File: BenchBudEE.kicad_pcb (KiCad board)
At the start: 4 copper layers, 165.1 x 63.5 mm, 134 parts, among them K1 1461069-5, P1 24-pin Mini-Fit Jr., P2 CONN_2, P3 CONN_3X2, P4 12-pin Terminal Block, P5 3-pin TB, Q1 2N3404, Q2 DMN65D8L-7, Q3 AOD476, Q4 AOD476, SW1 Power Switch, U1 LTV-816S, U10 LMT84, U11 OPA4170, U2 AP5726, U3 LM317T, U4 LM317T, U5 LM337T, U6 LM337T, U8 MCP4801, U9 MCP3901

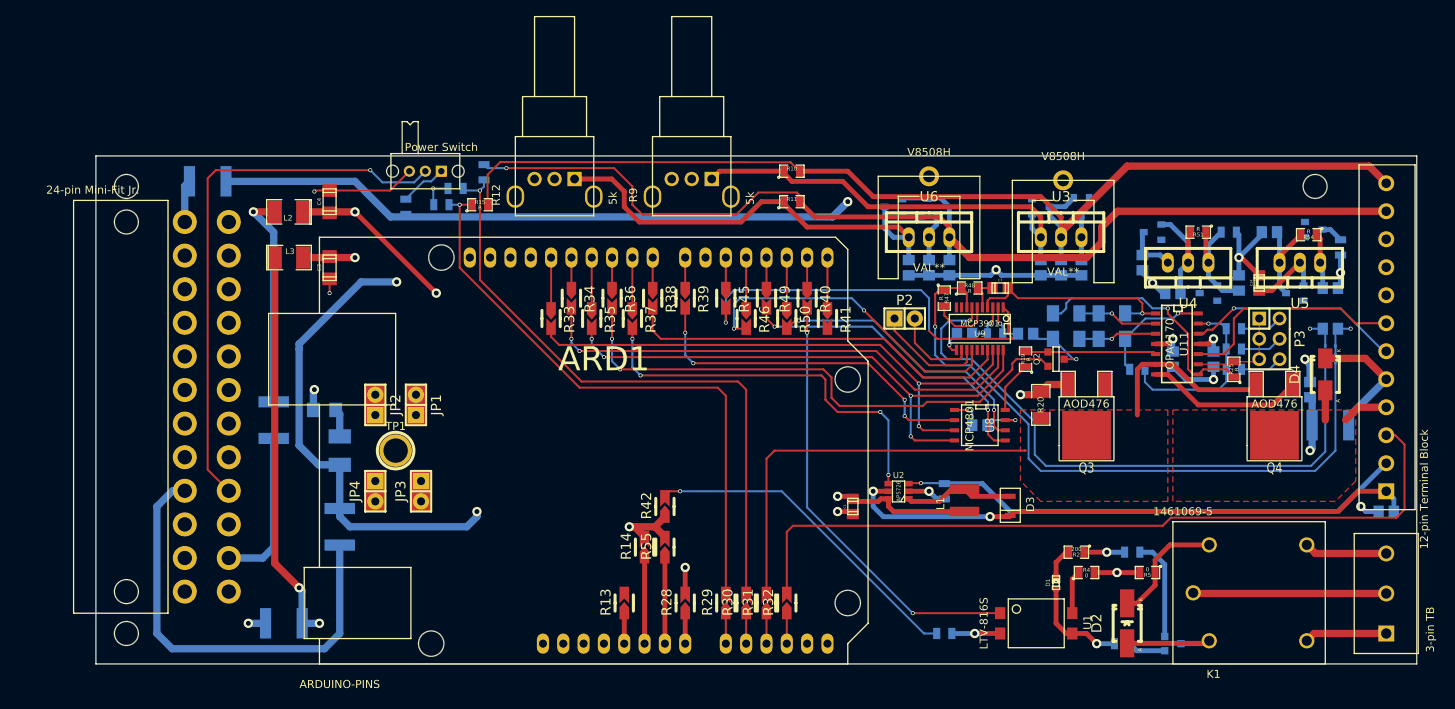
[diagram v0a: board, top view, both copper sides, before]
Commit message: Connected remaing nets
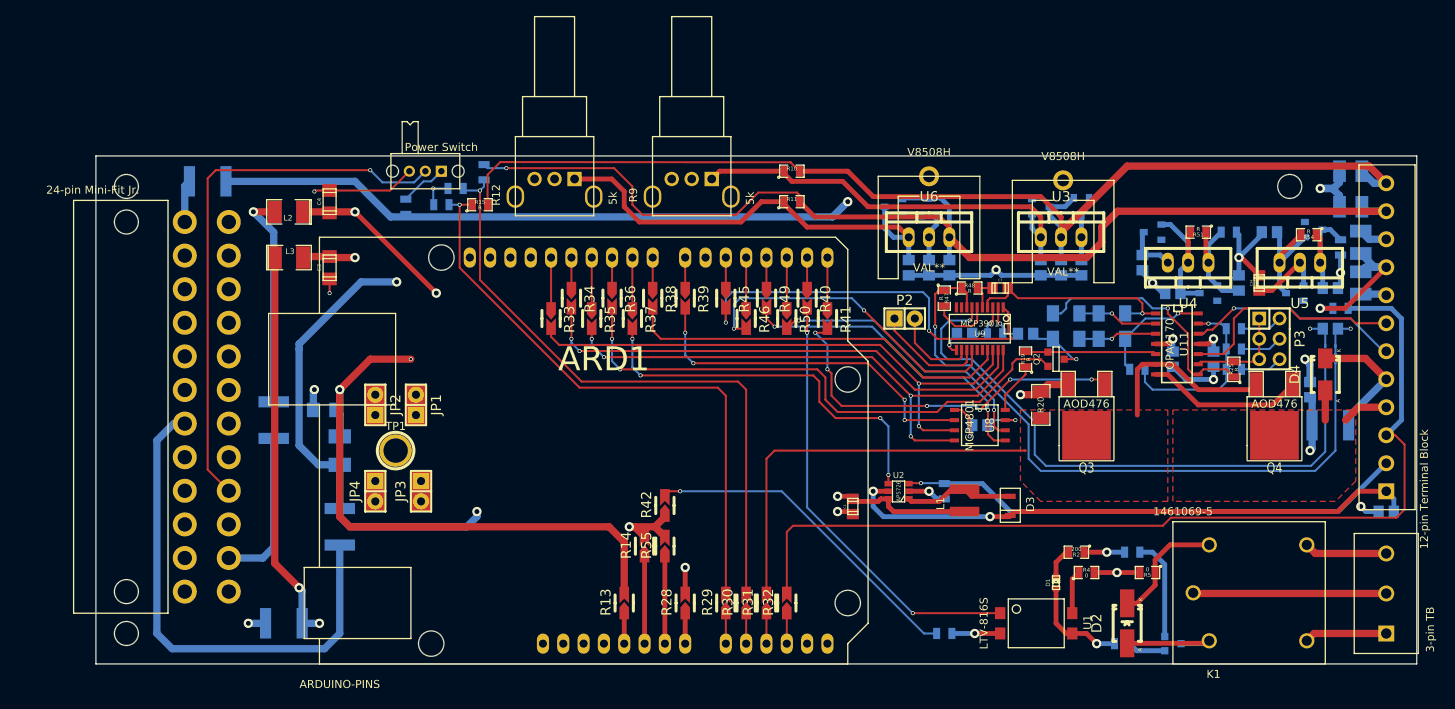
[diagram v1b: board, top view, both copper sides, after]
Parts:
- added C26: C, Capacitors_SMD:c_1210, B.Cu at (228.0, 52.7)
- added C27: C, Capacitors_SMD:c_1210, B.Cu at (228.0, 57.1)
- added C28: C, Capacitors_SMD:c_1210, B.Cu at (229.2, 61.6)
- added C29: C, Capacitors_SMD:c_1210, B.Cu at (229.2, 66.7)
- added R56: R, SMD_Packages:SM0805, B.Cu at (226.7, 69.8)
- moved 3 mm 3.18 mm to (220.3, 54.6)
- moved R14 0.13 mm to (139.7, 99.6)
- moved R42 0.13 mm to (142.2, 94.5)
- moved R55 0.13 mm to (142.2, 99.6)
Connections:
- P1 pad 2: Net-(P1-Pad12) -> Net-(P1-Pad2)
- P1 pad 6: Net-(P1-Pad4) -> Net-(P1-Pad6)
- TH2 pad 1: Net-(P1-Pad4) -> Net-(P1-Pad6)
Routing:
- net +5V: track 16.8 -> 94.4 mm, vias 3 -> 5
- net Net-(P1-Pad6): track 0.00 -> 64.0 mm
- net Net-(P1-Pad4): track 55.7 -> 0.00 mm
- net /Arduino/FAN_MODE: track 0.00 -> 47.2 mm, vias 0 -> 6
- net GND_PWR: track 26.1 -> 53.6 mm, vias 2 -> 4
- net /Fan/TACH_IN: track 96.9 -> 119.4 mm
- net FE_V-: track 29.8 -> 34.3 mm
- net Net-(C18-Pad2): track 9.77 -> 14.0 mm
- net /PowerAdjustmentMonitor/V+_ADJ: track 137.8 -> 141.5 mm
- net +3.3V: track 151.9 -> 155.5 mm
- net /PowerAdjustmentMonitor/V-_ADJ: track 139.1 -> 142.3 mm
- net +5P: track 214.8 -> 218.1 mm
- net FE_V+: track 29.3 -> 31.7 mm
- net /Arduino/FAN_PWM: track 68.1 -> 68.9 mm
- net /Arduino/~RESET: track 50.3 -> 50.1 mm, vias 1 -> 2

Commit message: Connected remaining ADC pins, some silk screen updates
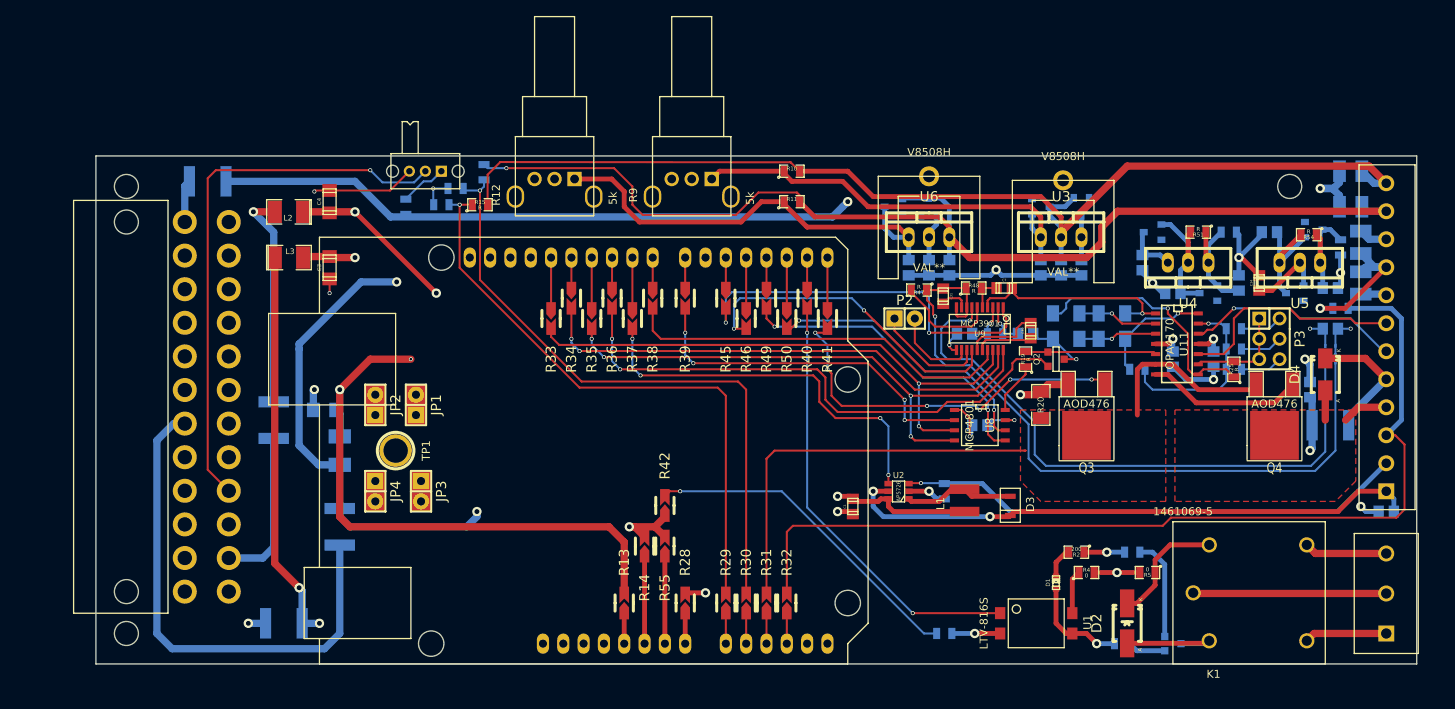
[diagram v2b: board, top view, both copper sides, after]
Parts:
- added C30: C, Capacitors_SMD:c_0805, F.Cu at (188.0, 72.6)
- added C31: C, Capacitors_SMD:c_0805, F.Cu at (177.0, 68.3)
- moved R47 3.33 mm to (174.0, 67.6), turned to 180 degrees
- moved R48 0.51 mm to (180.8, 67.3)
- moved C7 0.51 mm to (184.7, 67.3)
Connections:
- U9 pad 10: REF- -> AGND
- U9 pad 9: REF+ -> Net-(C31-Pad1)
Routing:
- net Net-(C30-Pad1): track 0.00 -> 9.29 mm
- net Net-(C30-Pad2): track 0.00 -> 7.24 mm
- net AGND: track 146.9 -> 153.2 mm
- net /Thermocouple/CH1-: track 7.86 -> 13.1 mm
- net Net-(C31-Pad1): track 0.00 -> 3.57 mm
- net /Arduino/~RESET: track 50.1 -> 47.7 mm
- net +12P: track 58.2 -> 57.6 mm
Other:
- net class Default: clearance 0.254 -> 0.1524
- rule pad_to_mask_clearance: 0 -> 0.0762
- rule trace_clearance: 0.254 -> 0.1524

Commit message: More silk screen tweaks
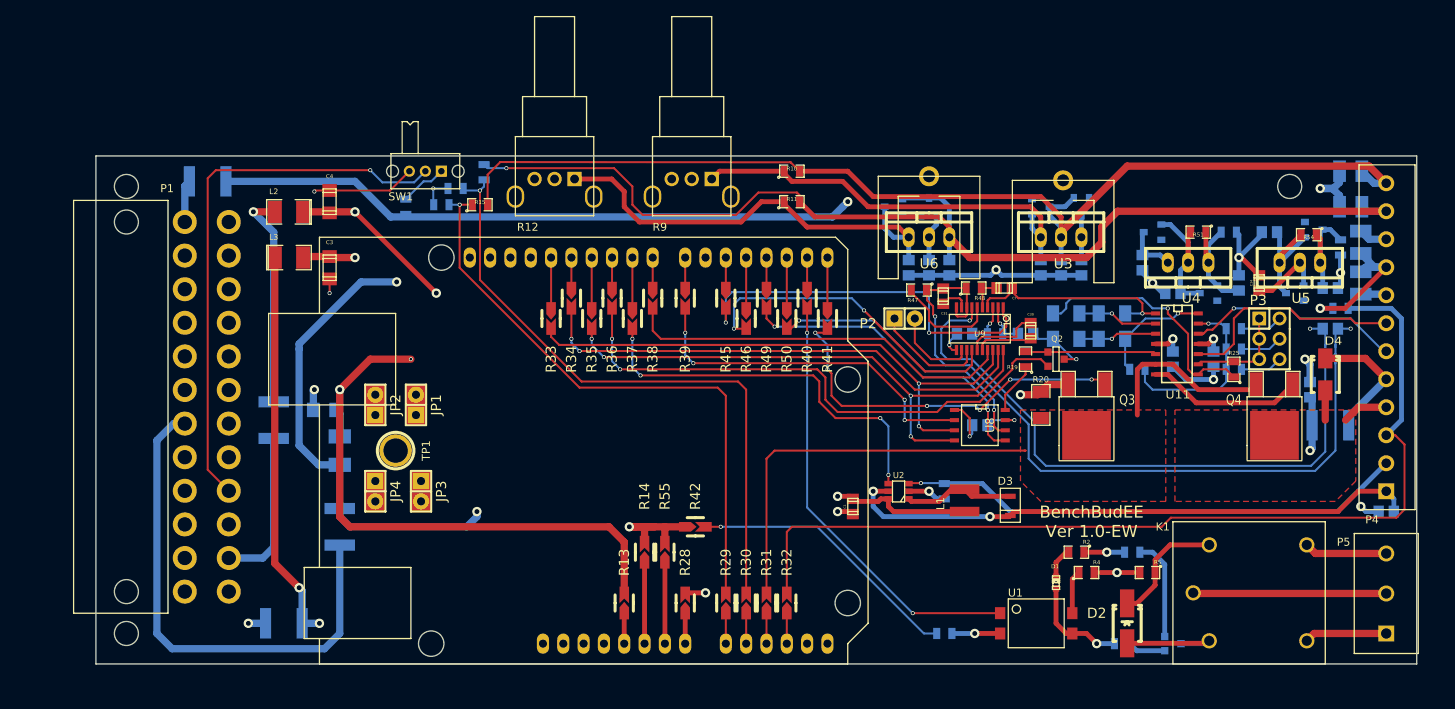
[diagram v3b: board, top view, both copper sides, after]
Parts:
- moved R42 4.65 mm to (146.1, 97.2), turned to 0 degrees
- moved R14 0.76 mm to (139.7, 100.3)
- moved R55 0.76 mm to (142.2, 100.3)
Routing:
- net /Arduino/RELAY-: track 41.6 -> 34.4 mm
- net GND: track 65.2 -> 70.7 mm
- net Net-(ARD1-Pad3): track 10.8 -> 10.0 mm
- net Net-(ARD1-Pad2): track 10.8 -> 10.0 mm
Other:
- board text added: "BenchBudEE Ver 1.0-EW"

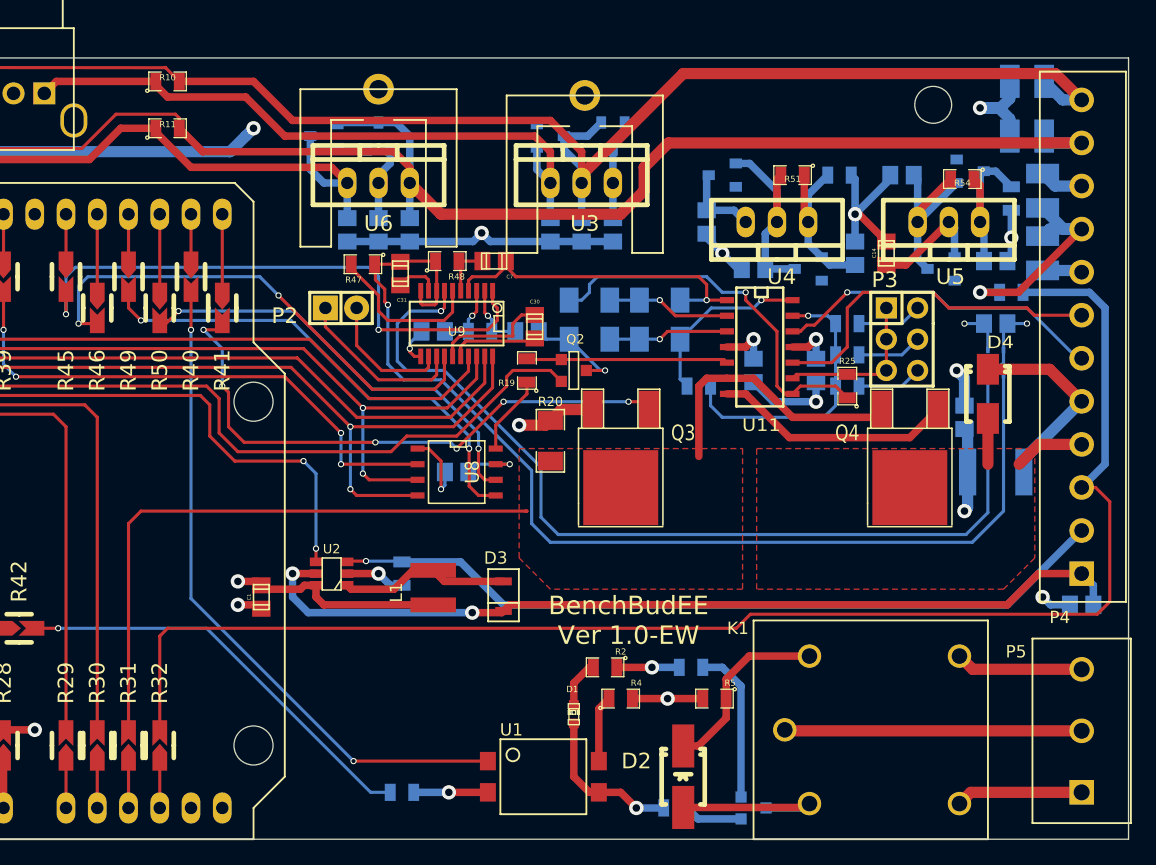
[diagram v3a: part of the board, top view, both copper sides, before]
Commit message: More small tweaks (cf. Layout Work Session 16)
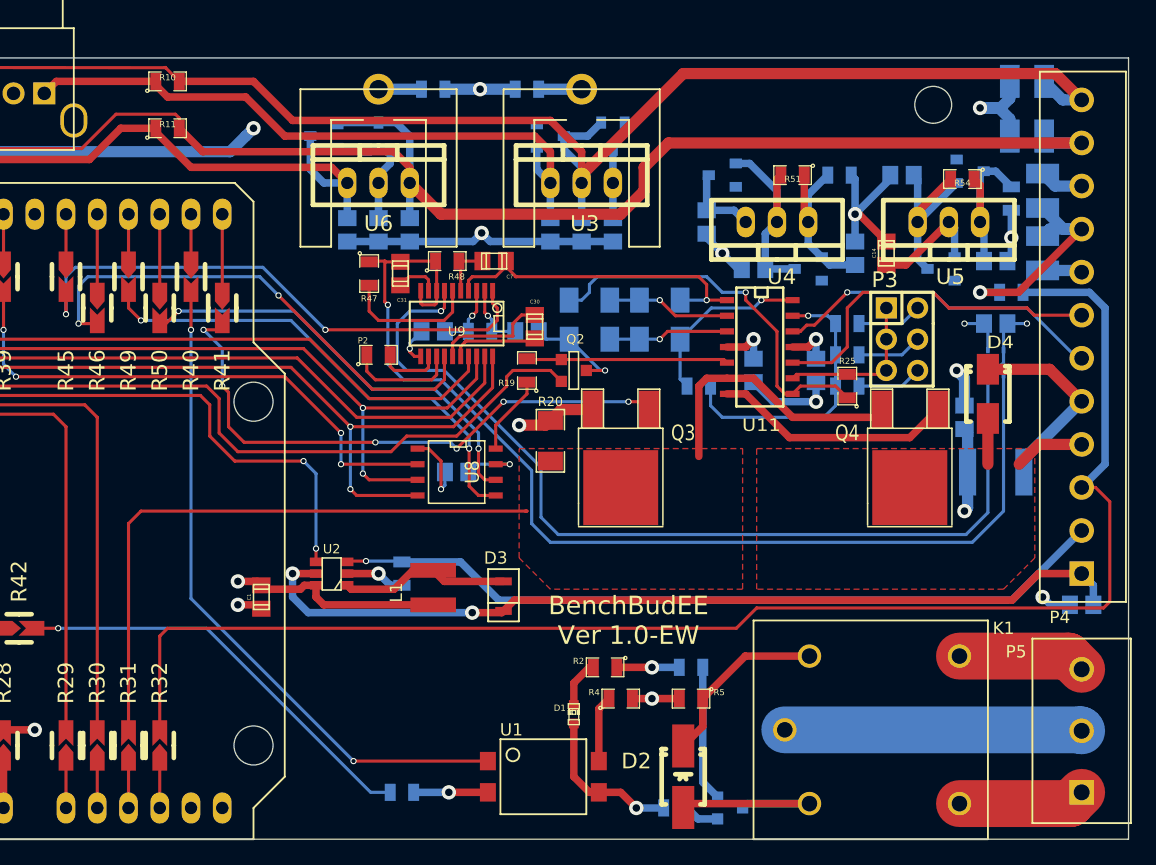
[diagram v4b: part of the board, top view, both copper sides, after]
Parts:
- removed V8508H (x2): VAL**, BenchBudEE:V8508H
- added P6: CONN_1, BenchBudEE:V8508H, F.Cu at (191.8, 53.3)
- added P7: CONN_1, BenchBudEE:V8508H, F.Cu at (175.3, 53.3)
- added R57: R, SMD_Packages:SM0805, B.Cu at (187.3, 53.3)
- added R58: R, SMD_Packages:SM0805, B.Cu at (179.7, 53.3)
- P2: footprint Pin_Headers:Pin_Header_Straight_1x02 -> SMD_Packages:SM0805
- moved P2 4.88 mm to (175.3, 74.9)
- moved Q1 1.91 mm to (203.8, 111.8)
- moved R5 1.91 mm to (200.7, 102.9)
- moved R47 0.92 mm to (174.5, 68.3), turned to 270 degrees
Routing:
- net GND_PWR: track 53.6 -> 59.4 mm, vias 4 -> 5
- net Net-(P2-Pad2): track 10.7 -> 5.19 mm
- net Net-(P2-Pad1): track 14.0 -> 8.97 mm
- net Net-(P7-Pad1): track 0.00 -> 3.49 mm
- net Net-(P6-Pad1): track 0.00 -> 3.49 mm
- net /Arduino/~RESET: track 47.7 -> 45.2 mm
- net Net-(Q1-Pad2): track 4.75 -> 2.84 mm
- net +12P: track 57.6 -> 55.7 mm
- net Net-(D2-Pad1): track 14.1 -> 16.0 mm
- net /Thermocouple/CH1-: track 13.1 -> 11.2 mm
- net Net-(Q1-Pad1): track 12.8 -> 11.0 mm
- net Net-(D2-Pad2): track 15.1 -> 14.6 mm
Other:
- net class AC added: clearance 1.524, trace_width 3.81, via_dia 1.1684, via_drill 0.6096
- rule pad_to_mask_clearance: 0.0762 -> 0
